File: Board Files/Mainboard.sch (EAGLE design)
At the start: 115 parts, among them J1 I2C Display

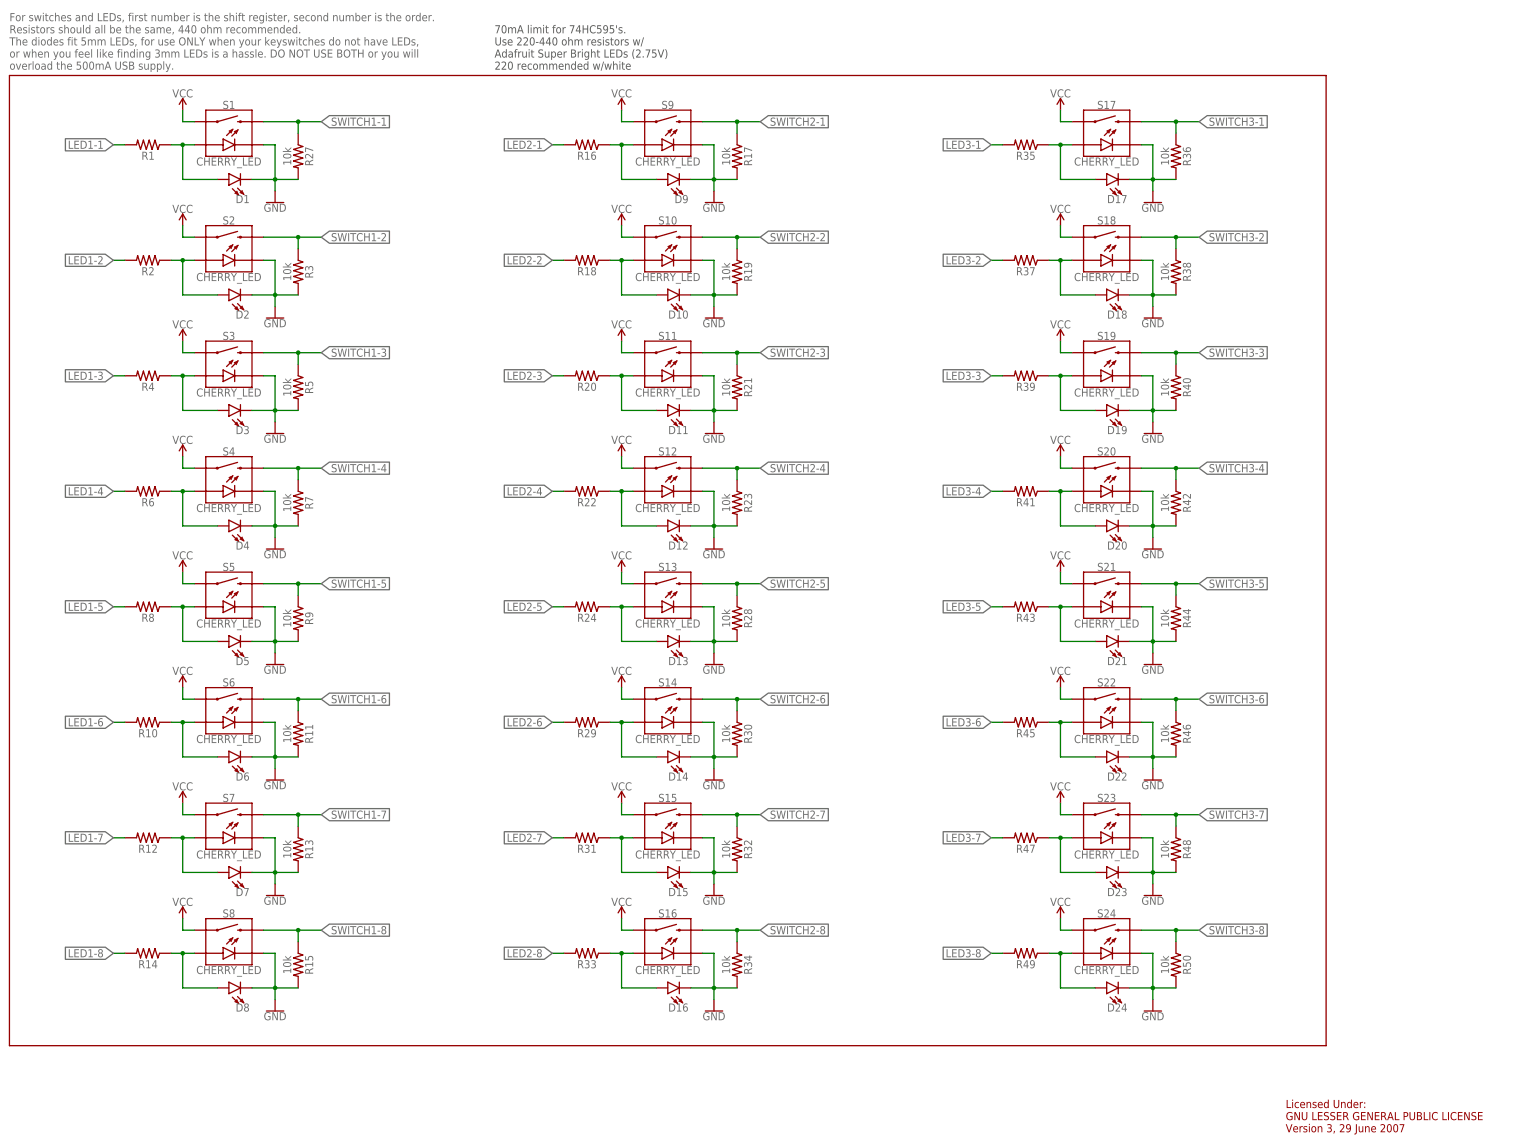
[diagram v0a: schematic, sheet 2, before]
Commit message: Board Layout Update
-Routed VCC and GND to white keys
-Routed GND to black keys
-Placed most components on board
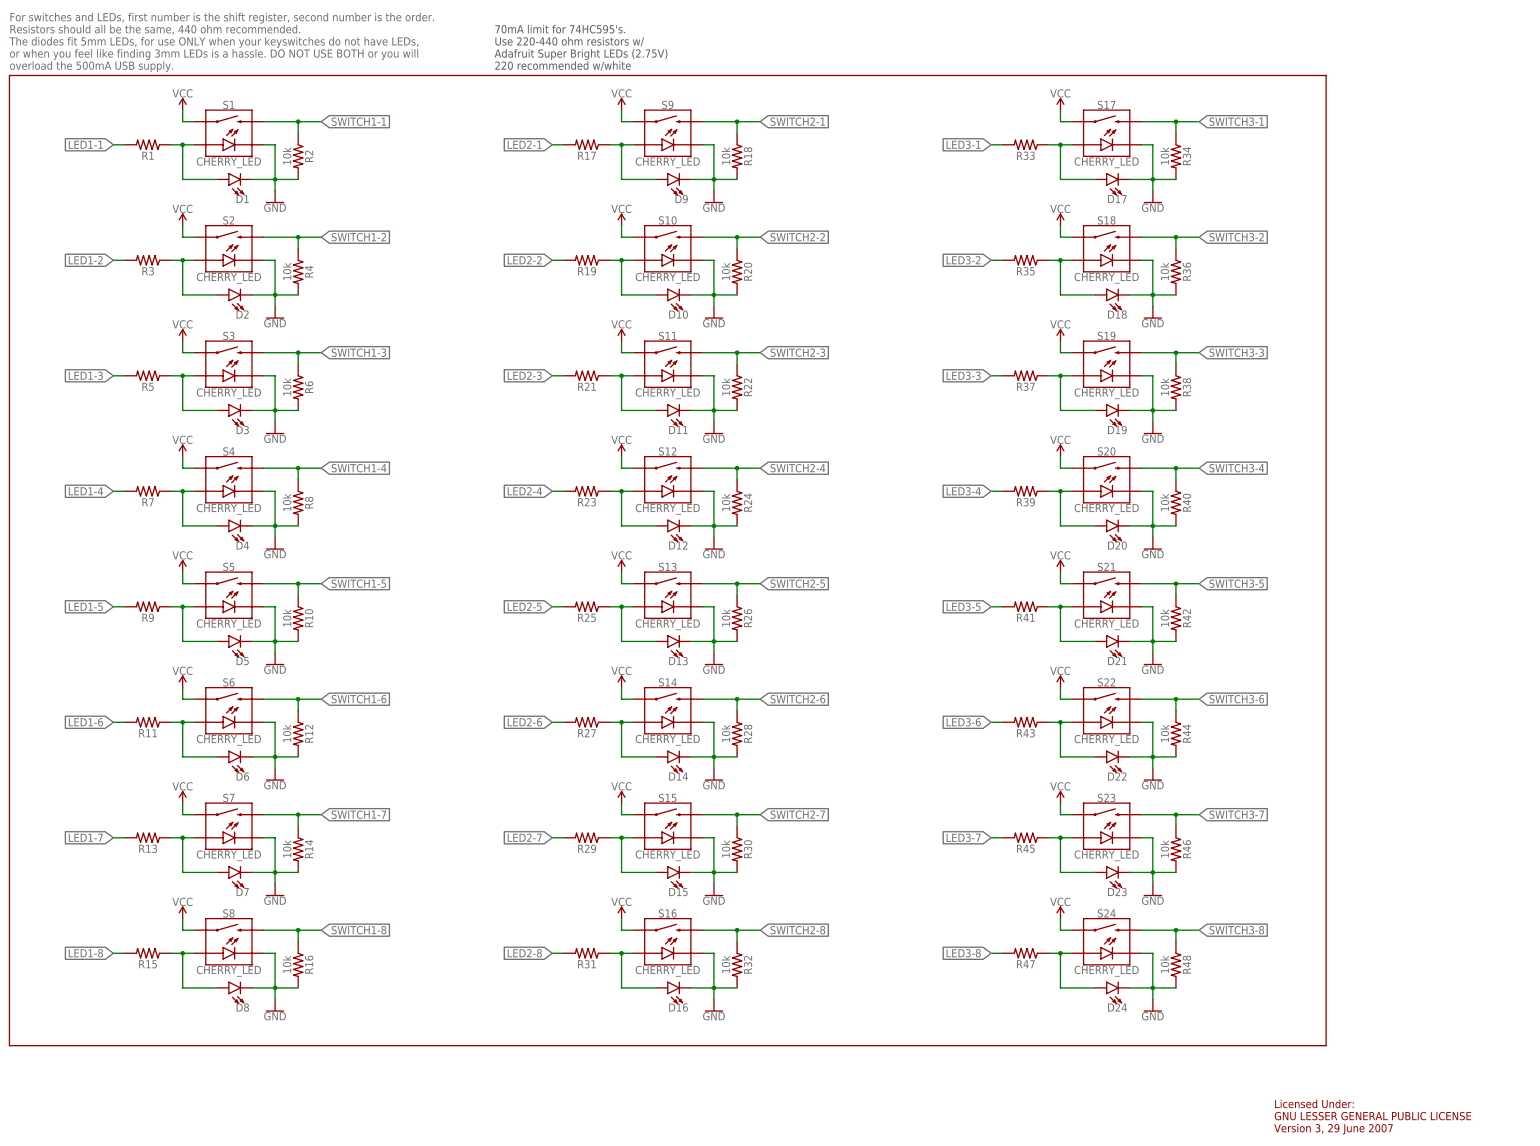
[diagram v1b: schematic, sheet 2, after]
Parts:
- R10, R12, R14, R16, R18, R2, R20, R22, R24, R4, R49, R6, R8: value (none) -> 10k; device SparkFun-Resistors:RESISTORAXIAL-0.3 -> SparkFun-Resistors:10KOHM-HORIZ-1/4W-1%
- R11, R13, R15, R17, R19, R21, R23, R25, R27, R3, R5, R7, R9: value 10k -> (none); device SparkFun-Resistors:10KOHM-HORIZ-1/4W-1% -> SparkFun-Resistors:RESISTORAXIAL-0.3
- VR1: device SparkFun-Resistors:POTENTIOMETER_SLIDE-20MM-1/10W-20% -> SparkFun-Resistors:POTENTIOMETER-PTH-9MM-1/20W-20%
- renumbered R55 to R53
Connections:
- net GND: now also R10.2, R12.2, R14.2, R16.2, R18.2, R2.2, R20.2, R22.2, R24.2, R26.2, R4.2, R49.1, R50.1, R6.2, R8.2; no longer R11.2, R13.2, R15.2, R17.2, R19.2, R21.2, R23.2, R27.2, R3.2, R5.2, R50.2, R51.1, R52.1, R7.2, R9.2
- net LED1-2: now also R3.2; no longer R2.2
- net LED1-3: now also R5.2; no longer R4.2
- net LED1-4: now also R7.2; no longer R6.2
- net LED1-5: now also R9.2; no longer R8.2
- net LED1-6: now also R11.2; no longer R10.2
- net LED1-7: now also R13.2; no longer R12.2
- net LED1-8: now also R15.2; no longer R14.2
- net LED2-1: now also R17.2; no longer R16.2
- net LED2-2: now also R19.2; no longer R18.2
- net LED2-3: now also R21.2; no longer R20.2
- net LED2-4: now also R23.2; no longer R22.2
- net LED2-5: now also R25.2; no longer R24.2
- net LED2-6: now also R27.2; no longer R29.2
- net LED2-7: now also R29.2; no longer R31.2
- net LED2-8: now also R31.2; no longer R33.2
- net LED3-1: now also R33.2; no longer R35.2
- net LED3-2: now also R35.2; no longer R37.2
- net LED3-3: now also R37.2; no longer R39.2
- net LED3-4: now also R39.2; no longer R41.2
- net LED3-5: now also R41.2; no longer R43.2
- net LED3-6: now also R43.2; no longer R45.2
- net LED3-7: now also R45.2; no longer R47.2
- net LED3-8: now also R47.2; no longer R49.2
- net N$10: now also R19.1; no longer R18.1
- net N$11: now also R21.1; no longer R20.1
- net N$12: now also R23.1; no longer R22.1
- net N$13: now also R25.1; no longer R24.1
- net N$14: now also R27.1; no longer R29.1
- net N$15: now also R29.1; no longer R31.1
- net N$16: now also R31.1; no longer R33.1
- net N$17: now also R33.1; no longer R35.1
- net N$18: now also R35.1; no longer R37.1
- net N$19: now also R37.1; no longer R39.1
- net N$2: now also R3.1; no longer R2.1
- net N$20: now also R39.1; no longer R41.1
- net N$21: now also R41.1; no longer R43.1
- net N$22: now also R43.1; no longer R45.1
- net N$23: now also R45.1; no longer R47.1
- net N$24: now also R47.1; no longer R49.1
- net N$3: now also R5.1; no longer R4.1
- net N$4: now also R7.1; no longer R6.1
- net N$5: now also R9.1; no longer R8.1
- net N$6: now also R11.1; no longer R10.1
- net N$7: now also R13.1; no longer R12.1
- net N$8: now also R15.1; no longer R14.1
- net N$9: now also R17.1; no longer R16.1
- net OCTAVE_DOWN: now also R50.2; no longer R52.2
- net OCTAVE_UP: now also R49.2; no longer R51.2
- net SCL: now also R51.1; no longer R25.1
- net SDA: now also R52.1; no longer R26.1
- net SWITCH1-1: now also R2.1; no longer R27.1
- net SWITCH1-2: now also R4.1; no longer R3.1
- net SWITCH1-3: now also R6.1; no longer R5.1
- net SWITCH1-4: now also R8.1; no longer R7.1
- net SWITCH1-5: now also R10.1; no longer R9.1
- net SWITCH1-6: now also R12.1; no longer R11.1
- net SWITCH1-7: now also R14.1; no longer R13.1
- net SWITCH1-8: now also R16.1; no longer R15.1
- net SWITCH2-1: now also R18.1; no longer R17.1
- net SWITCH2-2: now also R20.1; no longer R19.1
- net SWITCH2-3: now also R22.1; no longer R21.1
- net SWITCH2-4: now also R24.1; no longer R23.1
- net SWITCH2-5: now also R26.1; no longer R28.1
- net SWITCH2-6: now also R28.1; no longer R30.1
- net SWITCH2-7: now also R30.1; no longer R32.1
- net SWITCH2-8: now also R32.1; no longer R34.1
- net SWITCH3-1: now also R34.1; no longer R36.1
- net SWITCH3-2: now also R36.1; no longer R38.1
- net SWITCH3-3: now also R38.1; no longer R40.1
- net SWITCH3-4: now also R40.1; no longer R42.1
- net SWITCH3-5: now also R42.1; no longer R44.1
- net SWITCH3-6: now also R44.1; no longer R46.1
- net SWITCH3-7: now also R46.1; no longer R48.1
- net SWITCH3-8: now also R48.1; no longer R50.1
- net VCC: now also R51.2, R52.2; no longer R25.2, R26.2
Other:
- moved on the sheet: R10, R11, R12, R13, R14, R15, R16, R17, R18, R19, R2, R20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

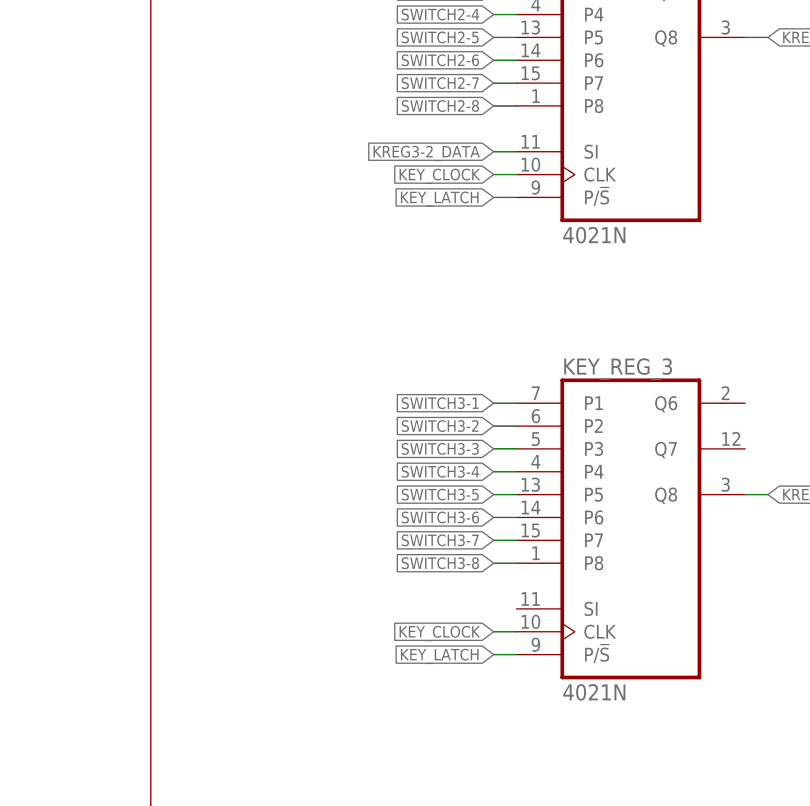
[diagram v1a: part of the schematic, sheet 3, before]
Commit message: Routed LEDs and most switches
-Routed all LEDs
-Routes 2/3rds of switches
-Probably need to reroute the right side
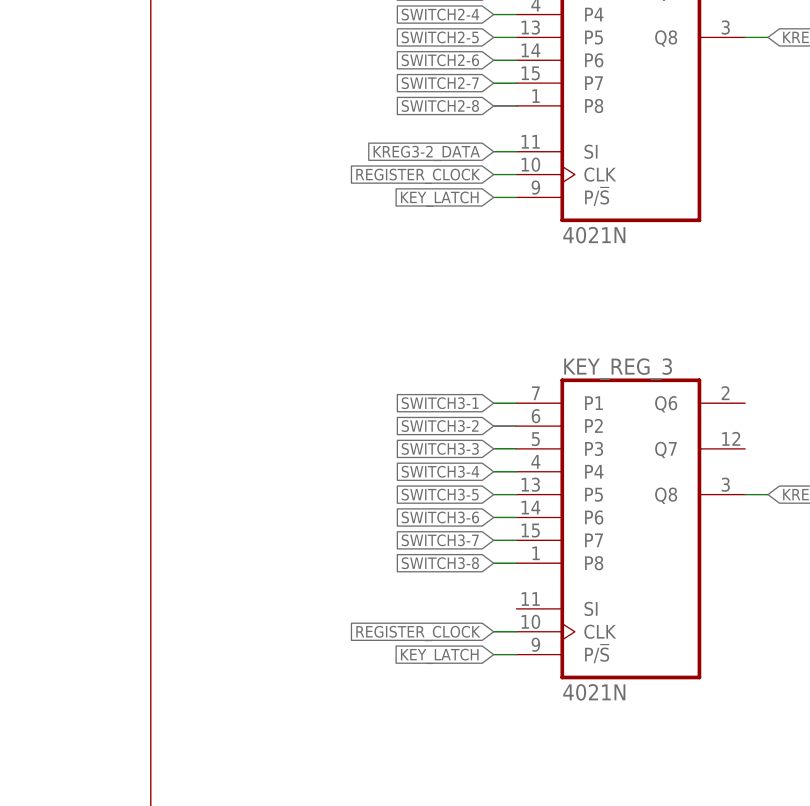
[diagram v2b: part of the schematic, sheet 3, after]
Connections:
- removed net KEY_CLOCK: KEY_REG_2A.CLK, KEY_REG_3A.CLK
- net REGISTER_CLOCK: now also KEY_REG_2A.CLK, KEY_REG_3A.CLK
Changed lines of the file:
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@@
 <?xml version="1.0" encoding="utf-8"?>
 <!DOCTYPE eagle SYSTEM "eagle.dtd">
-<eagle version="9.3.0">
+<eagle version="9.3.1">
 <drawing>
 <settings>
-<setting alwaysvectorfont="no"/>
+<setting alwaysvectorfont="yes"/>
 <setting verticaltext="up"/>
 </settings>
@@
 </segment>
 </net>
-<net name="KEY_CLOCK" class="0">
-<segment>
-<pinref part="KEY_REG_2" gate="A" pin="CLK"/>
-<wire x1="248.92" y1="124.46" x2="246.38" y2="124.46" width="0.1524" layer="91"/>
-<label x="246.38" y="124.46" size="1.27" layer="255" font="vector" rot="R180" xref="yes"/>
-</segment>
-<segment>
-<pinref part="KEY_REG_3" gate="A" pin="CLK"/>
-<wire x1="248.92" y1="73.66" x2="246.38" y2="73.66" width="0.1524" layer="91"/>
-<label x="246.38" y="73.66" size="1.27" layer="255" font="vector" rot="R180" xref="yes"/>
-</segment>
-</net>
 <net name="KEY_LATCH" class="0">
 <segment>
@@
 <label x="246.38" y="172.72" size="1.27" layer="255" font="vector" rot="R180" xref="yes"/>
 </segment>
+<segment>
+<pinref part="KEY_REG_2" gate="A" pin="CLK"/>
+<wire x1="248.92" y1="124.46" x2="246.38" y2="124.46" width="0.1524" layer="91"/>
+<label x="246.38" y="124.46" size="1.27" layer="255" font="vector" rot="R180" xref="yes"/>
+</segment>
+<segment>
+<pinref part="KEY_REG_3" gate="A" pin="CLK"/>
+<wire x1="248.92" y1="73.66" x2="246.38" y2="73.66" width="0.1524" layer="91"/>
+<label x="246.38" y="73.66" size="1.27" layer="255" font="vector" rot="R180" xref="yes"/>
+</segment>
 </net>
